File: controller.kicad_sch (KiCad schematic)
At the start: 1 part, among them U601 STM32L151C8Tx

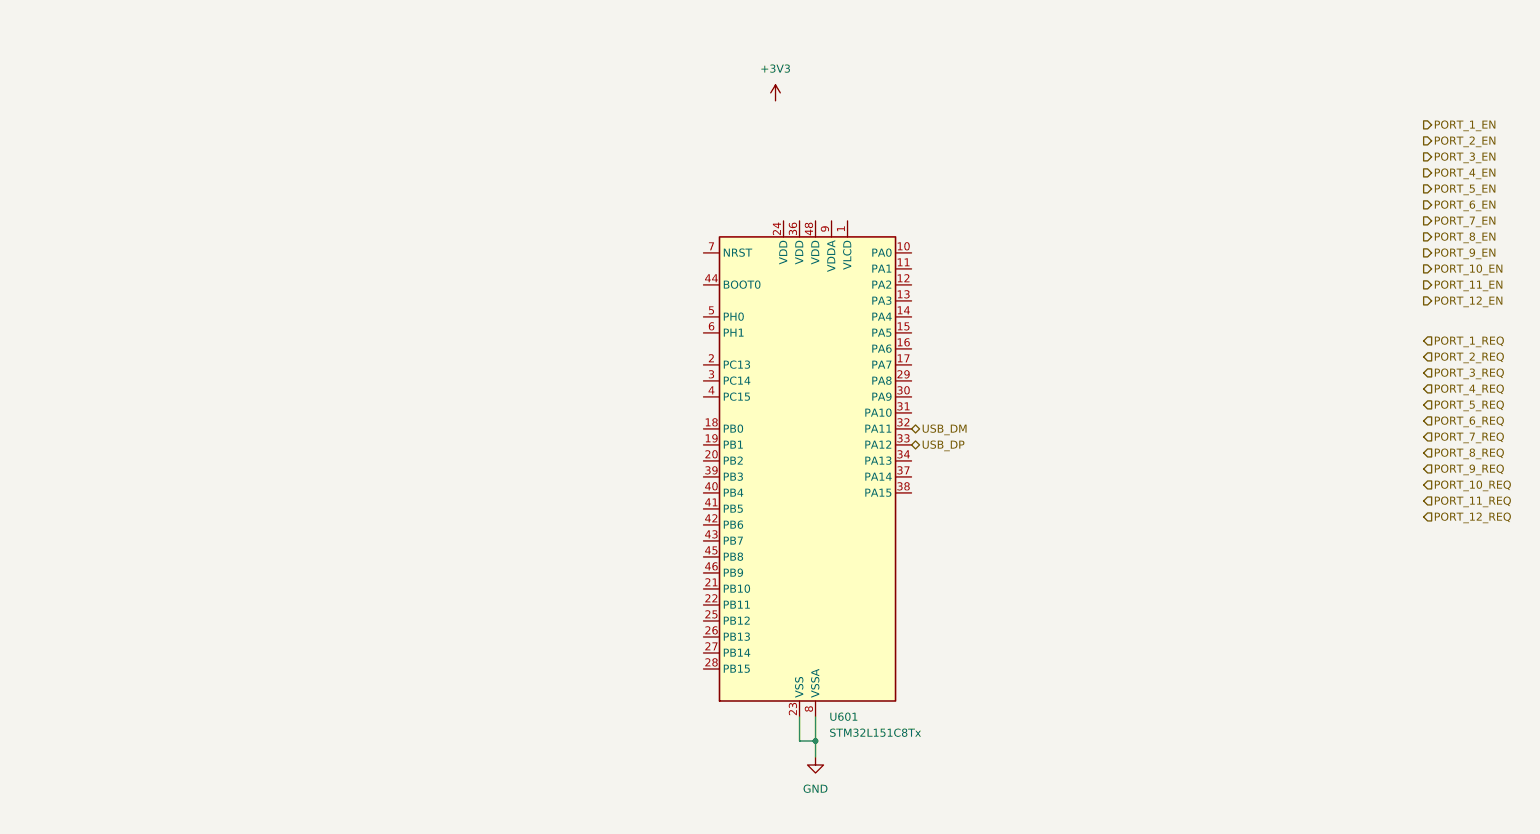
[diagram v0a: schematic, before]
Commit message: Add power management
And also some random stuff here and there
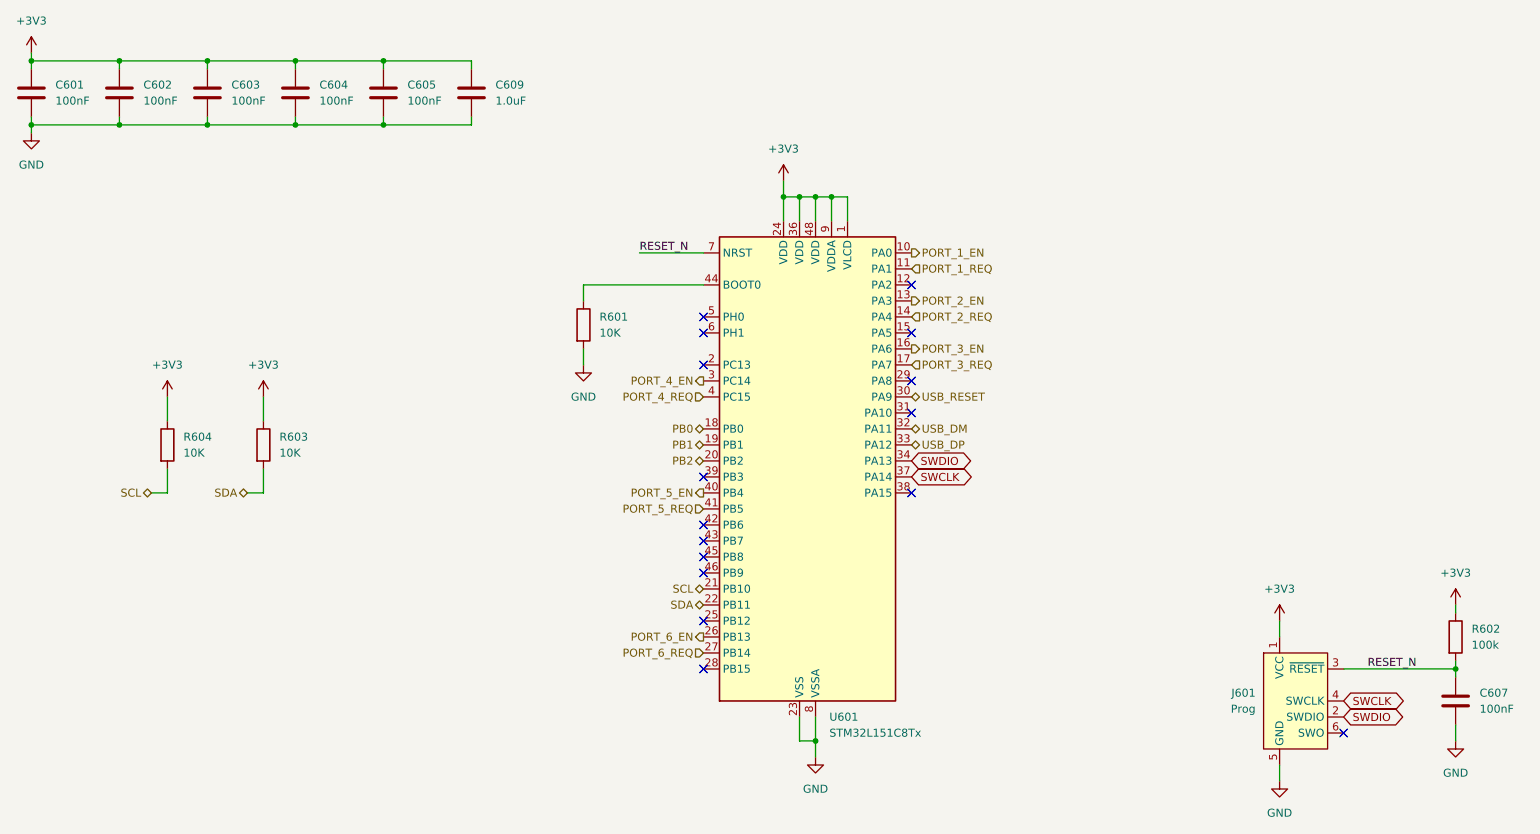
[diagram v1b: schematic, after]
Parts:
- added C601, C602, C603, C604, C605, C607: 100nF, Capacitor_SMD:C_0402_1005Metric, symbol Device:C
- added C609: 1.0uF, Capacitor_SMD:C_0402_1005Metric, symbol Device:C
- added J601: Prog, Connector:Tag-Connect_TC2030-IDC-NL_2x03_P1.27mm_Vertical, symbol Connector:Conn_ARM_SWD_TagConnect_TC2030-NL
- added R601, R603, R604: 10K, Resistor_SMD:R_0402_1005Metric, symbol Device:R
- added R602: 100k, Resistor_SMD:R_0402_1005Metric, symbol Device:R
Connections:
- net +3V3: now also U601.1 (VLCD), U601.24 (VDD), U601.36 (VDD), U601.48 (VDD), U601.9 (VDDA), C601.1, C602.1, C603.1, C604.1, C605.1, C609.1, J601.1 (VCC), R602.1, R603.1, R604.1
- net GND: now also C601.2, C602.2, C603.2, C604.2, C605.2, C607.2, C609.2, J601.5 (GND), R601.2
- net PORT_1_EN: now also U601.10 (PA0)
- net PORT_1_REQ: now also U601.11 (PA1)
- net PORT_2_EN: now also U601.13 (PA3)
- net PORT_2_REQ: now also U601.14 (PA4)
- net PORT_3_EN: now also U601.16 (PA6)
- net PORT_3_REQ: now also U601.17 (PA7)
- net PORT_4_EN: now also U601.3 (PC14)
- net PORT_4_REQ: now also U601.4 (PC15)
- net PORT_5_EN: now also U601.40 (PB4)
- net PORT_5_REQ: now also U601.41 (PB5)
- net PORT_6_EN: now also U601.26 (PB13)
- net PORT_6_REQ: now also U601.27 (PB14)
- net PB0: now reaches U601.18 (PB0)
- net PB1: now reaches U601.19 (PB1)
- net PB2: now reaches U601.20 (PB2)
- net SCL: now reaches U601.21 (PB10)
- net SCL: now also R604.2
- net SDA: now reaches U601.22 (PB11)
- net SDA: now also R603.2
- net USB_RESET: now reaches U601.30 (PA9)
- net SWDIO: now reaches U601.34 (PA13)
- net SWDIO: now also J601.2 (SWDIO)
- net SWCLK: now reaches U601.37 (PA14)
- net SWCLK: now also J601.4 (SWCLK)
- net at U601.44 (BOOT0): now also R601.1
- net RESET_N: now reaches U601.7 (NRST)
- net RESET_N: now also C607.1, J601.3 (~{RESET}), R602.2
- no-connect marks 0 -> 16

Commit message: Refine connectors and overall shape
Replace USB connectors, because of availability.
Use available barrel jack and USB-C connector instead of generic ones.
Update 3D Models

Refine rough placement of parts and board outline
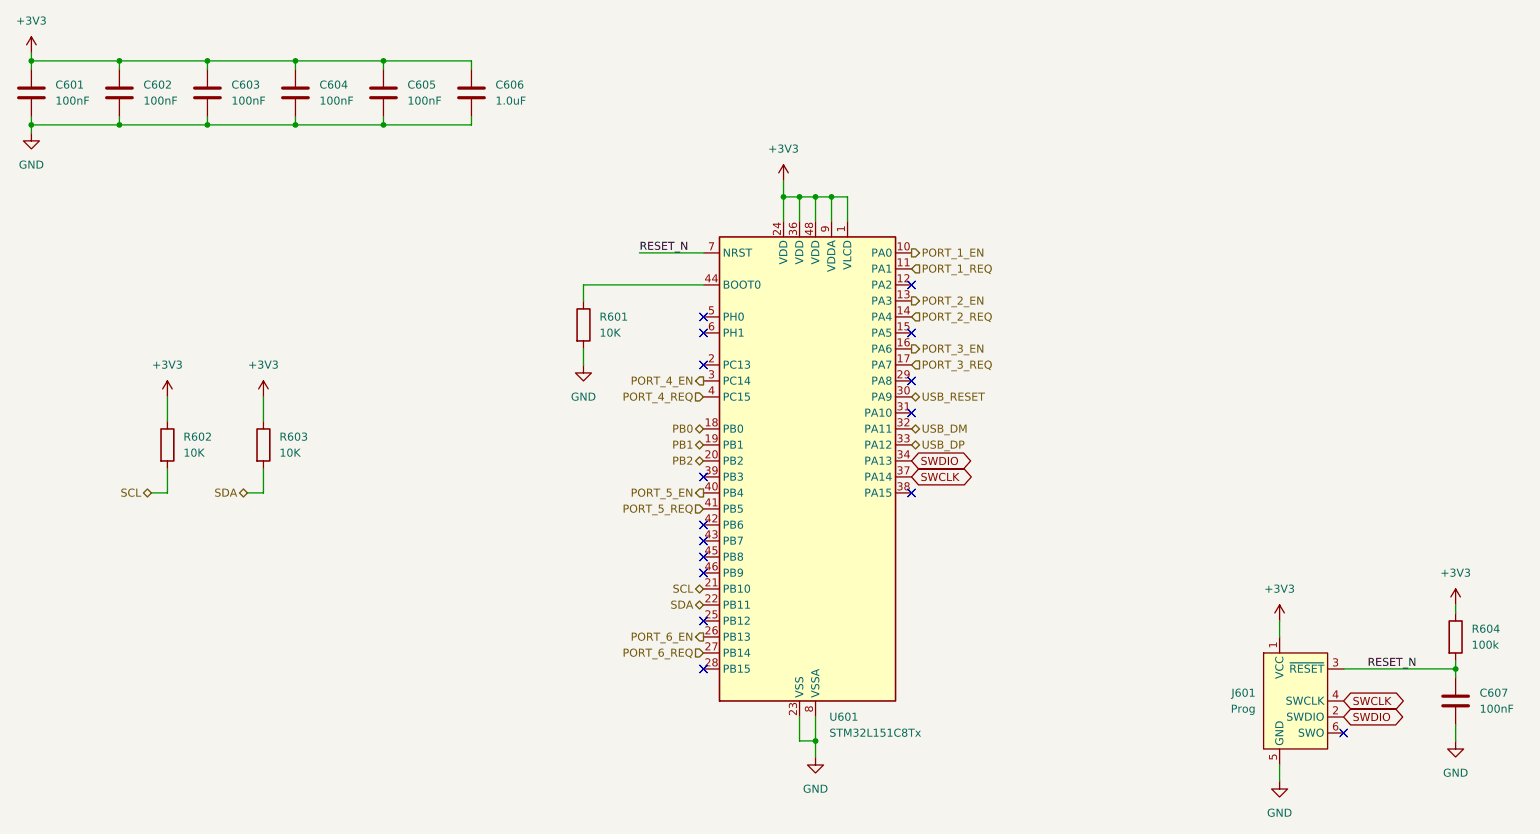
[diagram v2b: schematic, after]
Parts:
- C601, C602, C603, C604, C605, C607: LCSC# (none) -> C307331
- C606: renamed from C609; footprint Capacitor_SMD:C_0402_1005Metric -> Capacitor_SMD:C_0603_1608Metric; LCSC# (none) -> C15849
- J601: LCSC# (none) -> -
- R601, R603: LCSC# (none) -> C25744; MPN (none) -> 10k
- R602: renamed from R604; LCSC# (none) -> C25744; MPN (none) -> 10k
- R604: renamed from R602; LCSC# (none) -> C25741; MPN (none) -> 100K
- U601: MPN (none) -> STM32L151C8T6

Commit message: Finish first routing
Routed everything, so that the DRC and ERC do not show anything.
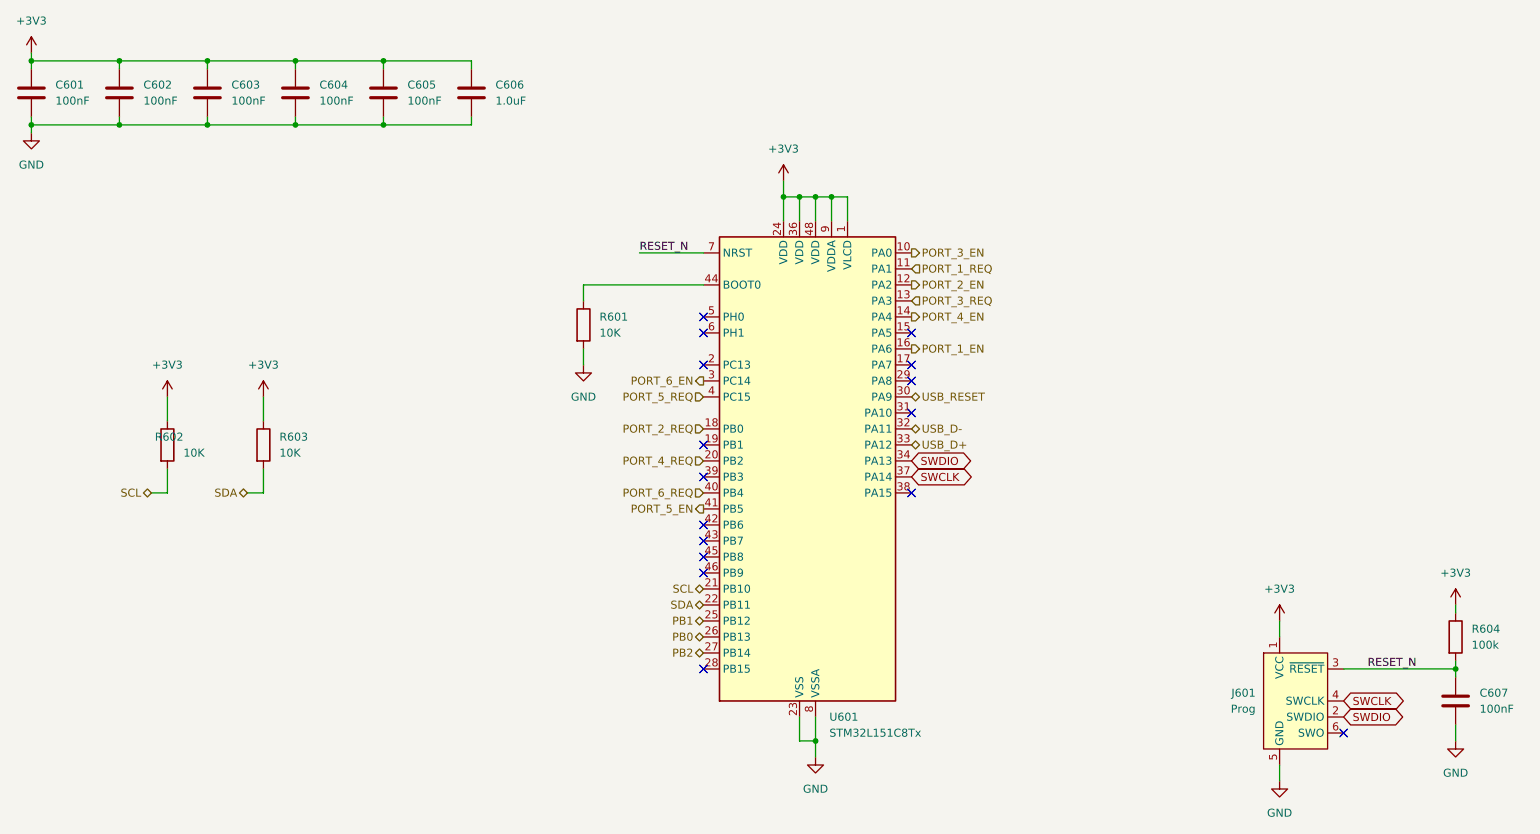
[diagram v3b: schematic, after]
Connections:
- net PB0: now also U601.26 (PB13); no longer U601.18 (PB0)
- net PB1: now also U601.25 (PB12); no longer U601.19 (PB1)
- net PB2: now also U601.27 (PB14); no longer U601.20 (PB2)
- net PORT_1_EN: now also U601.16 (PA6); no longer U601.10 (PA0)
- net PORT_2_EN: now also U601.12 (PA2); no longer U601.13 (PA3)
- net PORT_2_REQ: now also U601.18 (PB0); no longer U601.14 (PA4)
- net PORT_3_EN: now also U601.10 (PA0); no longer U601.16 (PA6)
- net PORT_3_REQ: now also U601.13 (PA3); no longer U601.17 (PA7)
- net PORT_4_EN: now also U601.14 (PA4); no longer U601.3 (PC14)
- net PORT_4_REQ: now also U601.20 (PB2); no longer U601.4 (PC15)
- net PORT_5_EN: now also U601.41 (PB5); no longer U601.40 (PB4)
- net PORT_5_REQ: now also U601.4 (PC15); no longer U601.41 (PB5)
- net PORT_6_EN: now also U601.3 (PC14); no longer U601.26 (PB13)
- net PORT_6_REQ: now also U601.40 (PB4); no longer U601.27 (PB14)
- net USB_DM renamed USB_D-
- net USB_DP renamed USB_D+
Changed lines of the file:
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@@
   (no_connect (at 125.73 64.77))
   (no_connect (at 125.73 62.23))
+  (no_connect (at 125.73 82.55))
   (no_connect (at 125.73 87.63))
   (no_connect (at 125.73 97.79))
   (no_connect (at 125.73 69.85))
-  (no_connect (at 125.73 110.49))
-  (no_connect (at 158.75 57.15))
+  (no_connect (at 158.75 69.85))
   (no_connect (at 227.33 128.27))
   (no_connect (at 125.73 118.11))
@@
     (effects (font (size 1.27 1.27)) (justify right))
   )
-  (hierarchical_label "PB2" (shape bidirectional) (at 125.73 85.09 180) (fields_autoplaced)
-    (effects (font (size 1.27 1.27)) (justify right))
-  )
-  (hierarchical_label "PORT_6_REQ" (shape input) (at 125.73 115.57 180) (fields_autoplaced)
-    (effects (font (size 1.27 1.27)) (justify right))
-  )
-  (hierarchical_label "PORT_4_REQ" (shape input) (at 125.73 74.93 180) (fields_autoplaced)
-    (effects (font (size 1.27 1.27)) (justify right))
-  )
-  (hierarchical_label "PORT_5_EN" (shape output) (at 125.73 90.17 180) (fields_autoplaced)
+  (hierarchical_label "PB2" (shape bidirectional) (at 125.73 115.57 180) (fields_autoplaced)
+    (effects (font (size 1.27 1.27)) (justify right))
+  )
+  (hierarchical_label "PORT_6_REQ" (shape input) (at 125.73 90.17 180) (fields_autoplaced)
+    (effects (font (size 1.27 1.27)) (justify right))
+  )
+  (hierarchical_label "PORT_4_REQ" (shape input) (at 125.73 85.09 180) (fields_autoplaced)
+    (effects (font (size 1.27 1.27)) (justify right))
+  )
+  (hierarchical_label "PORT_5_EN" (shape output) (at 125.73 92.71 180) (fields_autoplaced)
     (effects (font (size 1.27 1.27)) (justify right))
   )
@@
     (effects (font (size 1.27 1.27)) (justify right))
   )
-  (hierarchical_label "PORT_3_REQ" (shape input) (at 158.75 69.85 0) (fields_autoplaced)
-    (effects (font (size 1.27 1.27)) (justify left))
-  )
-  (hierarchical_label "USB_DP" (shape bidirectional) (at 158.75 82.55 0) (fields_autoplaced)
+  (hierarchical_label "PORT_3_REQ" (shape input) (at 158.75 59.69 0) (fields_autoplaced)
+    (effects (font (size 1.27 1.27)) (justify left))
+  )
+  (hierarchical_label "USB_D+" (shape bidirectional) (at 158.75 82.55 0) (fields_autoplaced)
     (effects (font (size 1.27 1.27)) (justify left))
   )
@@
     (effects (font (size 1.27 1.27)) (justify left))
   )
-  (hierarchical_label "PORT_5_REQ" (shape input) (at 125.73 92.71 180) (fields_autoplaced)
-    (effects (font (size 1.27 1.27)) (justify right))
-  )
-  (hierarchical_label "PB1" (shape bidirectional) (at 125.73 82.55 180) (fields_autoplaced)
+  (hierarchical_label "PORT_5_REQ" (shape input) (at 125.73 74.93 180) (fields_autoplaced)
+    (effects (font (size 1.27 1.27)) (justify right))
+  )
+  (hierarchical_label "PB1" (shape bidirectional) (at 125.73 110.49 180) (fields_autoplaced)
     (effects (font (size 1.27 1.27)) (justify right))
   )
@@
     (effects (font (size 1.27 1.27)) (justify right))
   )
-  (hierarchical_label "PORT_3_EN" (shape output) (at 158.75 67.31 0) (fields_autoplaced)
-    (effects (font (size 1.27 1.27)) (justify left))
-  )
-  (hierarchical_label "PB0" (shape bidirectional) (at 125.73 80.01 180) (fields_autoplaced)
+  (hierarchical_label "PORT_3_EN" (shape output) (at 158.75 52.07 0) (fields_autoplaced)
+    (effects (font (size 1.27 1.27)) (justify left))
+  )
+  (hierarchical_label "PB0" (shape bidirectional) (at 125.73 113.03 180) (fields_autoplaced)
     (effects (font (size 1.27 1.27)) (justify right))
   )
@@
     (effects (font (size 1.27 1.27)) (justify right))
   )
-  (hierarchical_label "USB_DM" (shape bidirectional) (at 158.75 80.01 0) (fields_autoplaced)
-    (effects (font (size 1.27 1.27)) (justify left))
-  )
-  (hierarchical_label "PORT_2_REQ" (shape input) (at 158.75 62.23 0) (fields_autoplaced)
-    (effects (font (size 1.27 1.27)) (justify left))
-  )
-  (hierarchical_label "PORT_6_EN" (shape output) (at 125.73 113.03 180) (fields_autoplaced)
+  (hierarchical_label "USB_D-" (shape bidirectional) (at 158.75 80.01 0) (fields_autoplaced)
+    (effects (font (size 1.27 1.27)) (justify left))
+  )
+  (hierarchical_label "PORT_2_REQ" (shape input) (at 125.73 80.01 180) (fields_autoplaced)
+    (effects (font (size 1.27 1.27)) (justify right))
+  )
+  (hierarchical_label "PORT_6_EN" (shape output) (at 125.73 72.39 180) (fields_autoplaced)
     (effects (font (size 1.27 1.27)) (justify right))
   )
@@
     (effects (font (size 1.27 1.27)) (justify left))
   )
-  (hierarchical_label "PORT_2_EN" (shape output) (at 158.75 59.69 0) (fields_autoplaced)
-    (effects (font (size 1.27 1.27)) (justify left))
-  )
-  (hierarchical_label "PORT_4_EN" (shape output) (at 125.73 72.39 180) (fields_autoplaced)
-    (effects (font (size 1.27 1.27)) (justify right))
-  )
-  (hierarchical_label "PORT_1_EN" (shape output) (at 158.75 52.07 0) (fields_autoplaced)
+  (hierarchical_label "PORT_2_EN" (shape output) (at 158.75 57.15 0) (fields_autoplaced)
+    (effects (font (size 1.27 1.27)) (justify left))
+  )
+  (hierarchical_label "PORT_4_EN" (shape output) (at 158.75 62.23 0) (fields_autoplaced)
+    (effects (font (size 1.27 1.27)) (justify left))
+  )
+  (hierarchical_label "PORT_1_EN" (shape output) (at 158.75 67.31 0) (fields_autoplaced)
     (effects (font (size 1.27 1.27)) (justify left))
   )
@@
   )
   (symbol (lib_id "Device:R") (at 40.64 82.55 0) (unit 1)
-    (in_bom yes) (on_board yes) (dnp no) (fields_autoplaced)
+    (in_bom yes) (on_board yes) (dnp no)
     (property "Reference" "R602" (at 43.18 81.28 0)
-      (effects (font (size 1.27 1.27)) (justify left))
+      (effects (font (size 1.27 1.27)) (justify right))
     )
     (property "Value" "10K" (at 43.18 83.82 0)
